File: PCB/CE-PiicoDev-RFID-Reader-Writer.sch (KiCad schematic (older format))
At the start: 59 parts, among them J1 , J2 , J3 Conn_01x06_Male, SW1 SW_DIP_x02, U1 MFRC522, Y1 27.12MHz 12pF

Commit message: Update
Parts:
- removed G4: Label_PCB_Art, PiicoDev RFID MFRC522:Label_Reset_Bar_Reverse Arrow, symbol CoreElectronics_Artwork:Label_PCB_Art
- removed G5: Label_PCB_Art, PiicoDev RFID MFRC522:Label_Reset_Bar, symbol CoreElectronics_Artwork:Label_PCB_Art
- U1: footprint Package_DFN_QFN:VQFN-32-1EP_5x5mm_P0.5mm_EP3.1x3.1mm -> Package_DFN_QFN:VQFN-32-1EP_5x5mm_P0.5mm_EP3.1x3.1mm_ThermalVias
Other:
- note removed: "~RST"
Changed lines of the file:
@@
 Sheet 1 1
 Title "PiicoDev RFID Reader/Writer MFRC522"
-Date "2021-12-14"
+Date "2021-12-21"
 Rev "03"
 Comp "Core Electronics"
@@
 	5450 1750 5850 1750
 Connection ~ 5850 1750
-$Comp
-L power:GND #PWR0112
-U 1 1 6156B677
-P 5100 2650
-F 0 "#PWR0112" H 5100 2400 50  0001 C CNN
-F 1 "GND" H 5105 2477 50  0000 C CNN
-F 2 "" H 5100 2650 50  0001 C CNN
-F 3 "" H 5100 2650 50  0001 C CNN
-	1    5100 2650
-	1    0    0    -1
-$EndComp
 Wire Wire Line
 	5100 2650 5100 2600
@@
 F 0 "U1" H 6050 1627 50  0000 C CNN
 F 1 "MFRC522" H 6050 1536 50  0000 C CNN
-F 2 "Package_DFN_QFN:VQFN-32-1EP_5x5mm_P0.5mm_EP3.1x3.1mm" H 5900 3350 50  0001 C CNN
+F 2 "Package_DFN_QFN:VQFN-32-1EP_5x5mm_P0.5mm_EP3.1x3.1mm_ThermalVias" H 5900 3350 50  0001 C CNN
 F 3 "https://www.nxp.com/docs/en/data-sheet/MFRC522.pdf" H 5900 3350 50  0001 C CNN
 	1    6050 3150
@@
 Text Label 10400 3150 0    50   ~ 0
 TURN6A
-$Comp
-L CoreElectronics_Artwork:Label_PCB_Art G4
-U 1 1 617897A9
-P 4150 6900
-F 0 "G4" H 4278 6946 50  0000 L CNN
-F 1 "Label_PCB_Art" H 4278 6855 50  0000 L CNN
-F 2 "PiicoDev RFID MFRC522:Label_Reset_Bar_Reverse Arrow" H 4150 6900 50  0001 C CNN
-F 3 "" H 4150 6900 50  0001 C CNN
-	1    4150 6900
-	1    0    0    -1
-$EndComp
-$Comp
-L CoreElectronics_Artwork:Label_PCB_Art G5
-U 1 1 6178A645
-P 4150 7150
-F 0 "G5" H 4278 7196 50  0000 L CNN
-F 1 "Label_PCB_Art" H 4278 7105 50  0000 L CNN
-F 2 "PiicoDev RFID MFRC522:Label_Reset_Bar" H 4150 7150 50  0001 C CNN
-F 3 "" H 4150 7150 50  0001 C CNN
-	1    4150 7150
-	1    0    0    -1
-$EndComp
-Text Notes 4050 6950 0    50   ~ 0
-~RST
-Text Notes 4050 7200 0    50   ~ 0
-~RST
 Text Notes 4050 5300 0    50   ~ 0
 f = 13.56 MHz\n\nCoil (as measured)\nL = 470 nH\nR = 0.3 ohm
@@
 U 1 1 61AFBFE8
 P 5100 2950
-F 0 "R11" V 4893 2950 50  0000 C CNN
-F 1 "120R" V 4984 2950 50  0000 C CNN
+F 0 "R11" V 5100 2950 50  0000 C CNN
+F 1 "120R" V 5200 2950 50  0000 C CNN
 F 2 "Resistor_SMD:R_0402_1005Metric" V 5030 2950 50  0001 C CNN
 F 3 "~" H 5100 2950 50  0001 C CNN
@@
 Wire Wire Line
 	2600 1800 2800 1800
+$Comp
+L power:GND #PWR0112
+U 1 1 6156B677
+P 5100 2650
+F 0 "#PWR0112" H 5100 2400 50  0001 C CNN
+F 1 "GND" H 5100 2500 50  0000 C CNN
+F 2 "" H 5100 2650 50  0001 C CNN
+F 3 "" H 5100 2650 50  0001 C CNN
+	1    5100 2650
+	1    0    0    -1
+$EndComp
 $EndSCHEMATC

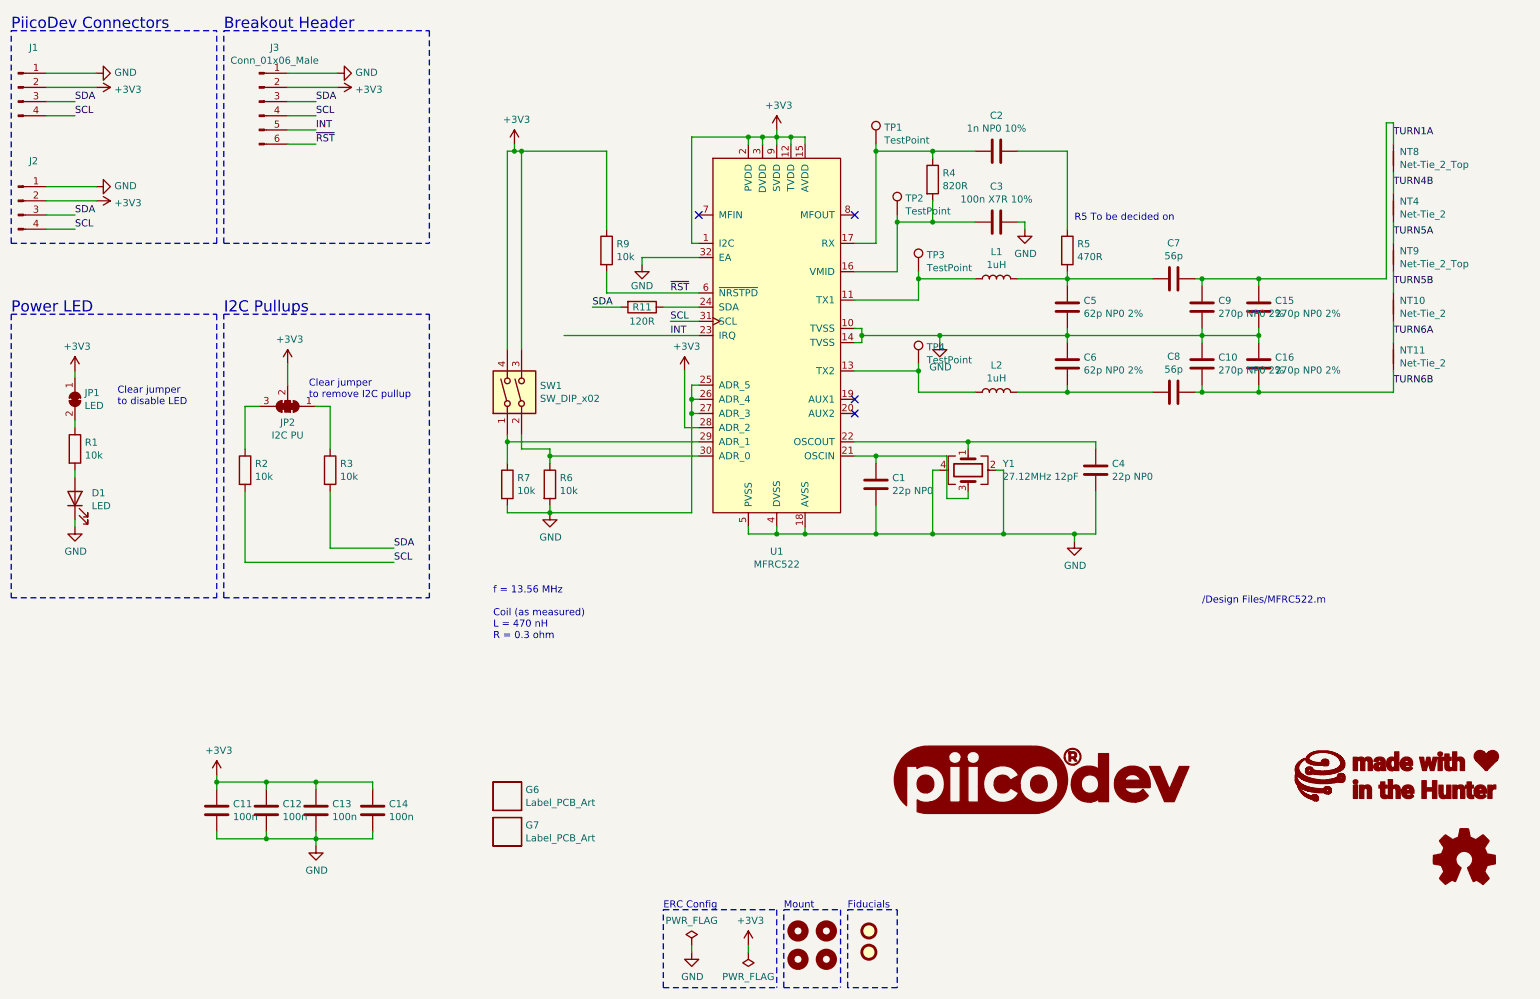
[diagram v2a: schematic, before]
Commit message: v10 Release
Remove testpoints
Change ASW order so SW1 is LSB
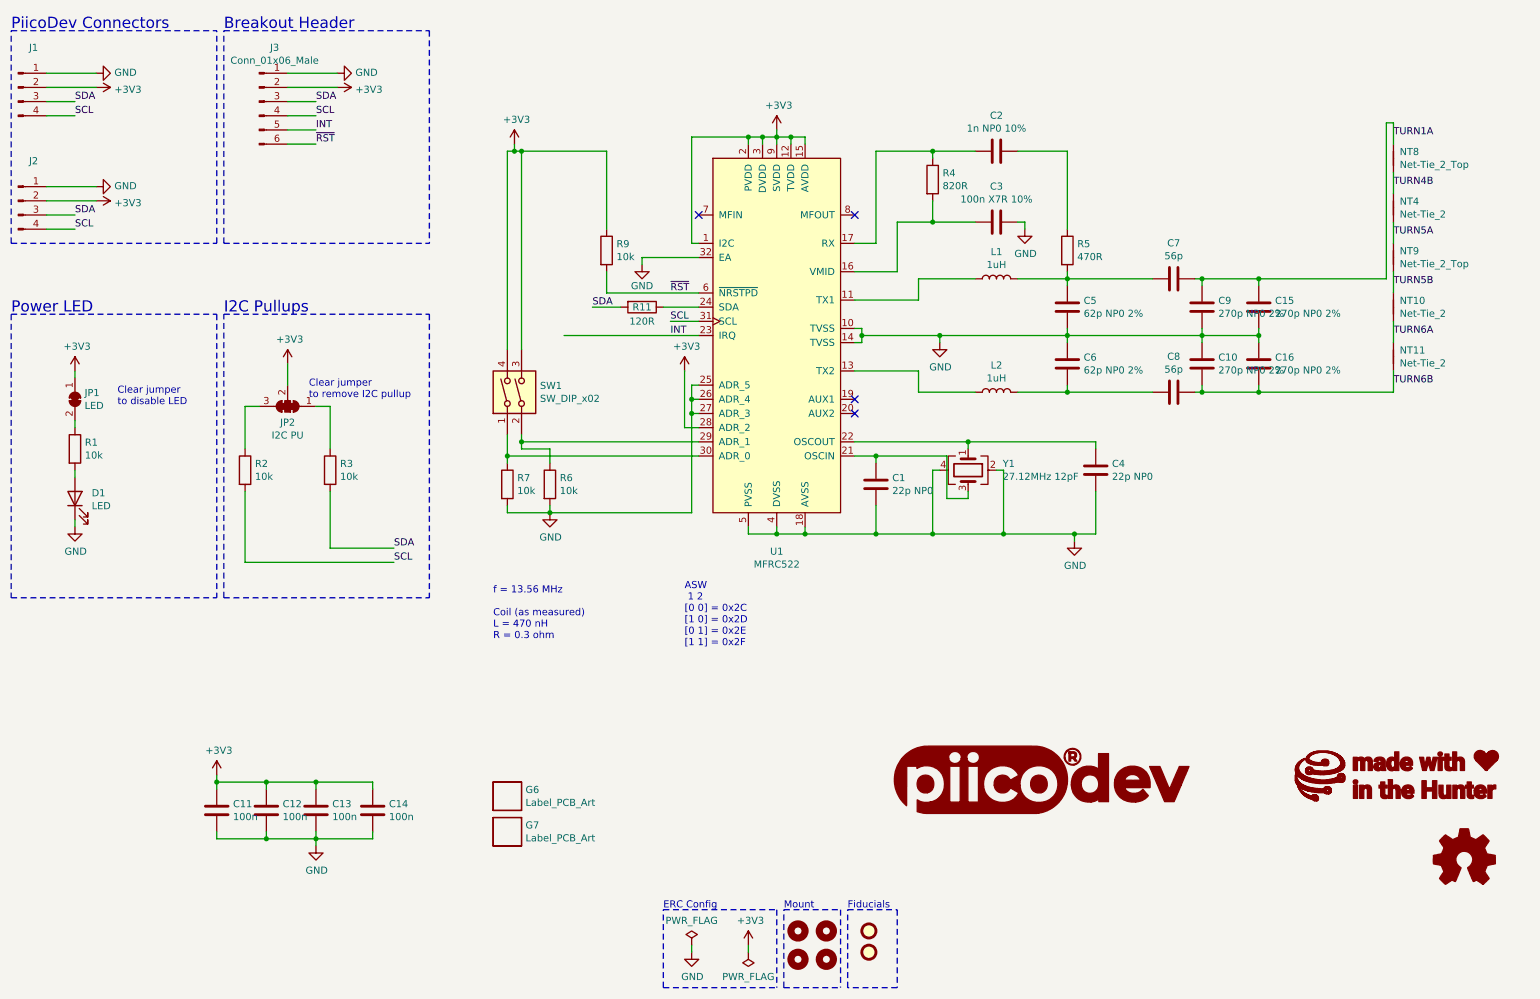
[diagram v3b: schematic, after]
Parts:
- removed TP1, TP2, TP3, TP4: TestPoint, CoreElectronics_Components:TestPoint_Pad_0.7x0.7mm, symbol Connector:TestPoint
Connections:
- net at R7.1, SW1.1: now also U1.30 (ADR_0); no longer U1.29 (ADR_1)
- net at R6.1, SW1.2: now also U1.29 (ADR_1); no longer U1.30 (ADR_0)
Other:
- note added: "ASW\n 1 2\n[0 0] = 0x2C\n[1 0] = 0x2D\n[0 1] = 0x2E\n[1 1] = 0x2F"
- note removed: "/Design Files/MFRC522.m"
- note removed: "R5 To be decided on"
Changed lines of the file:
@@
 encoding utf-8
 Sheet 1 1
-Title "PiicoDev RFID Reader/Writer MFRC522"
-Date "2021-12-23"
-Rev "04"
+Title "PiicoDev RFID Module"
+Date "2022-01-12"
+Rev "10"
 Comp "Core Electronics"
 Comment1 "Designed at Core Electronics by Peter Johnston"
@@
 Wire Wire Line
 	8100 3550 8700 3550
-Text Notes 8150 2350 0    50   ~ 0
-R5 To be decided on
 Wire Wire Line
 	6050 1750 6150 1750
@@
 Text Notes 4050 5300 0    50   ~ 0
 f = 13.56 MHz\n\nCoil (as measured)\nL = 470 nH\nR = 0.3 ohm
-Text Notes 9050 5050 0    50   ~ 0
-/Design Files/MFRC522.m
 Wire Wire Line
 	4850 2850 5500 2850
@@
 Wire Wire Line
 	4950 2950 4750 2950
-$Comp
-L Connector:TestPoint TP3
-U 1 1 618A1A4D
-P 7050 2700
-F 0 "TP3" H 7108 2818 50  0000 L CNN
-F 1 "TestPoint" H 7108 2727 50  0000 L CNN
-F 2 "CoreElectronics_Components:TestPoint_Pad_0.7x0.7mm" H 7250 2700 50  0001 C CNN
-F 3 "~" H 7250 2700 50  0001 C CNN
-	1    7050 2700
-	1    0    0    -1
-$EndComp
-$Comp
-L Connector:TestPoint TP4
-U 1 1 618A2E15
-P 7050 3350
-F 0 "TP4" H 7108 3468 50  0000 L CNN
-F 1 "TestPoint" H 7108 3377 50  0000 L CNN
-F 2 "CoreElectronics_Components:TestPoint_Pad_0.7x0.7mm" H 7250 3350 50  0001 C CNN
-F 3 "~" H 7250 3350 50  0001 C CNN
-	1    7050 3350
-	1    0    0    -1
-$EndComp
-Wire Wire Line
-	7050 2700 7050 2750
-Connection ~ 7050 2750
-Wire Wire Line
-	7050 3350 7050 3400
-Connection ~ 7050 3400
-$Comp
-L Connector:TestPoint TP1
-U 1 1 618B17E8
-P 6750 1800
-F 0 "TP1" H 6808 1918 50  0000 L CNN
-F 1 "TestPoint" H 6808 1827 50  0000 L CNN
-F 2 "CoreElectronics_Components:TestPoint_Pad_0.7x0.7mm" H 6950 1800 50  0001 C CNN
-F 3 "~" H 6950 1800 50  0001 C CNN
-	1    6750 1800
-	1    0    0    -1
-$EndComp
-Wire Wire Line
-	6750 1800 6750 1850
-Connection ~ 6750 1850
-$Comp
-L Connector:TestPoint TP2
-U 1 1 618B9830
-P 6900 2300
-F 0 "TP2" H 6958 2418 50  0000 L CNN
-F 1 "TestPoint" H 6958 2327 50  0000 L CNN
-F 2 "CoreElectronics_Components:TestPoint_Pad_0.7x0.7mm" H 7100 2300 50  0001 C CNN
-F 3 "~" H 7100 2300 50  0001 C CNN
-	1    6900 2300
-	1    0    0    -1
-$EndComp
-Wire Wire Line
-	6900 2300 6900 2350
-Connection ~ 6900 2350
 Wire Wire Line
 	5500 3500 5450 3500
@@
 $EndComp
 Wire Wire Line
-	5500 4000 4450 4000
-Wire Wire Line
-	4450 4000 4450 4050
-Wire Wire Line
 	4450 4350 4450 4400
-Connection ~ 4450 4000
 $Comp
 L CoreElectronics_Artwork:Label_PCB_Art G7
@@
 	4250 1850 4850 1850
 Wire Wire Line
-	4150 3850 4150 3900
-Wire Wire Line
-	4150 3900 4150 4050
-Connection ~ 4150 3900
-Wire Wire Line
-	4250 3850 4250 3950
+	4250 3850 4250 3900
 Wire Wire Line
 	4250 3950 4450 3950
-Wire Wire Line
-	4450 3950 4450 4000
-Wire Wire Line
-	4150 3900 5500 3900
 Wire Wire Line
 	5450 3700 5450 4400
@@
 	1    0    0    -1
 $EndComp
+Text Notes 5400 5350 0    50   ~ 0
+ ASW\n 1 2\n[0 0] = 0x2C\n[1 0] = 0x2D\n[0 1] = 0x2E\n[1 1] = 0x2F
+Wire Wire Line
+	4450 3950 4450 4050
+Wire Wire Line
+	5500 4000 4150 4000
+Connection ~ 4150 4000
+Wire Wire Line
+	4150 4000 4150 4050
+Wire Wire Line
+	4150 3850 4150 4000
+Wire Wire Line
+	5500 3900 4250 3900
+Connection ~ 4250 3900
+Wire Wire Line
+	4250 3900 4250 3950
 $EndSCHEMATC

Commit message: Change R5 to 1k
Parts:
- R5: value 470R -> 1k
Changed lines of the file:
@@
 P 8100 2550
 F 0 "R5" H 8170 2596 50  0000 L CNN
-F 1 "470R" H 8170 2505 50  0000 L CNN
+F 1 "1k" H 8170 2505 50  0000 L CNN
 F 2 "Resistor_SMD:R_0603_1608Metric" V 8030 2550 50  0001 C CNN
 F 3 "~" H 8100 2550 50  0001 C CNN

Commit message: Add schematic.pdf and schematic comments
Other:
- note added: "ASW I2C ADDR\n 1 2\n[0 0] = 0x2C\n[1 0] = 0x2D\n[0 1] = 0x2E\n[1 1] = 0x2F"
- note added: "Net ties allow coil dimensions\nto be prescribed in PCB layout"
- note removed: "ASW\n 1 2\n[0 0] = 0x2C\n[1 0] = 0x2D\n[0 1] = 0x2E\n[1 1] = 0x2F"
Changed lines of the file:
@@
 P 5450 7450
 AR Path="/609C5735/609C9ECA" Ref="#FLG?"  Part="1"
-AR Path="/609C9ECA" Ref="#FLG0101"  Part="1"
-F 0 "#FLG0101" H 5450 7525 50  0001 C CNN
+AR Path="/609C9ECA" Ref="#FLG?"  Part="1"
+F 0 "#FLG?" H 5450 7525 50  0001 C CNN
 F 1 "PWR_FLAG" H 5450 7623 50  0000 C CNN
 F 2 "" H 5450 7450 50  0001 C CNN
@@
 P 5850 7500
 AR Path="/609C5735/609C9ED0" Ref="#FLG?"  Part="1"
-AR Path="/609C9ED0" Ref="#FLG0102"  Part="1"
-F 0 "#FLG0102" H 5850 7575 50  0001 C CNN
+AR Path="/609C9ED0" Ref="#FLG?"  Part="1"
+F 0 "#FLG?" H 5850 7575 50  0001 C CNN
 F 1 "PWR_FLAG" H 5850 7673 50  0000 C CNN
 F 2 "" H 5850 7500 50  0001 C CNN
@@
 P 5450 7500
 AR Path="/609C5735/609C9ED6" Ref="#PWR?"  Part="1"
-AR Path="/609C9ED6" Ref="#PWR0101"  Part="1"
-F 0 "#PWR0101" H 5450 7250 50  0001 C CNN
+AR Path="/609C9ED6" Ref="#PWR?"  Part="1"
+F 0 "#PWR?" H 5450 7250 50  0001 C CNN
 F 1 "GND" H 5455 7327 50  0000 C CNN
 F 2 "" H 5450 7500 50  0001 C CNN
@@
 P 5850 7450
 AR Path="/609C5735/609C9EDC" Ref="#PWR?"  Part="1"
-AR Path="/609C9EDC" Ref="#PWR0102"  Part="1"
-F 0 "#PWR0102" H 5850 7300 50  0001 C CNN
+AR Path="/609C9EDC" Ref="#PWR?"  Part="1"
+F 0 "#PWR?" H 5850 7300 50  0001 C CNN
 F 1 "+3V3" H 5865 7623 50  0000 C CNN
 F 2 "" H 5850 7450 50  0001 C CNN
@@
 P 1250 1400
 AR Path="/609C5735/609F9AF4" Ref="#PWR?"  Part="1"
-AR Path="/609F9AF4" Ref="#PWR0103"  Part="1"
-F 0 "#PWR0103" H 1250 1250 50  0001 C CNN
+AR Path="/609F9AF4" Ref="#PWR?"  Part="1"
+F 0 "#PWR?" H 1250 1250 50  0001 C CNN
 F 1 "+3V3" V 1265 1528 50  0000 L CNN
 F 2 "" H 1250 1400 50  0001 C CNN
@@
 P 1250 1300
 AR Path="/609C5735/609F9AFA" Ref="#PWR?"  Part="1"
-AR Path="/609F9AFA" Ref="#PWR0104"  Part="1"
-F 0 "#PWR0104" H 1250 1050 50  0001 C CNN
+AR Path="/609F9AFA" Ref="#PWR?"  Part="1"
+F 0 "#PWR?" H 1250 1050 50  0001 C CNN
 F 1 "GND" V 1255 1172 50  0000 R CNN
 F 2 "" H 1250 1300 50  0001 C CNN
@@
 P 1250 2200
 AR Path="/609C5735/609F9B0C" Ref="#PWR?"  Part="1"
-AR Path="/609F9B0C" Ref="#PWR0105"  Part="1"
-F 0 "#PWR0105" H 1250 2050 50  0001 C CNN
+AR Path="/609F9B0C" Ref="#PWR?"  Part="1"
+F 0 "#PWR?" H 1250 2050 50  0001 C CNN
 F 1 "+3V3" V 1265 2328 50  0000 L CNN
 F 2 "" H 1250 2200 50  0001 C CNN
@@
 P 1250 2100
 AR Path="/609C5735/609F9B12" Ref="#PWR?"  Part="1"
-AR Path="/609F9B12" Ref="#PWR0106"  Part="1"
-F 0 "#PWR0106" H 1250 1850 50  0001 C CNN
+AR Path="/609F9B12" Ref="#PWR?"  Part="1"
+F 0 "#PWR?" H 1250 1850 50  0001 C CNN
 F 1 "GND" V 1255 1972 50  0000 R CNN
 F 2 "" H 1250 2100 50  0001 C CNN
@@
 P 2950 1400
 AR Path="/609C5735/609F9B1E" Ref="#PWR?"  Part="1"
-AR Path="/609F9B1E" Ref="#PWR0107"  Part="1"
-F 0 "#PWR0107" H 2950 1250 50  0001 C CNN
+AR Path="/609F9B1E" Ref="#PWR?"  Part="1"
+F 0 "#PWR?" H 2950 1250 50  0001 C CNN
 F 1 "+3V3" V 2965 1528 50  0000 L CNN
 F 2 "" H 2950 1400 50  0001 C CNN
@@
 P 2950 1300
 AR Path="/609C5735/609F9B24" Ref="#PWR?"  Part="1"
-AR Path="/609F9B24" Ref="#PWR0108"  Part="1"
-F 0 "#PWR0108" H 2950 1050 50  0001 C CNN
+AR Path="/609F9B24" Ref="#PWR?"  Part="1"
+F 0 "#PWR?" H 2950 1050 50  0001 C CNN
 F 1 "GND" V 2955 1172 50  0000 R CNN
 F 2 "" H 2950 1300 50  0001 C CNN
@@
 P 2600 3350
 AR Path="/609C5735/60A0817C" Ref="#PWR?"  Part="1"
-AR Path="/60A0817C" Ref="#PWR0109"  Part="1"
-F 0 "#PWR0109" H 2600 3200 50  0001 C CNN
+AR Path="/60A0817C" Ref="#PWR?"  Part="1"
+F 0 "#PWR?" H 2600 3200 50  0001 C CNN
 F 1 "+3V3" H 2615 3523 50  0000 C CNN
 F 2 "" H 2600 3350 50  0001 C CNN
@@
 $EndComp
 $Comp
-L power:GND #PWR0110
+L power:GND #PWR?
 U 1 1 60A1F608
 P 1100 4500
-F 0 "#PWR0110" H 1100 4250 50  0001 C CNN
+F 0 "#PWR?" H 1100 4250 50  0001 C CNN
 F 1 "GND" H 1105 4327 50  0000 C CNN
 F 2 "" H 1100 4500 50  0001 C CNN
@@
 	1100 4500 1100 4450
 $Comp
-L power:+3V3 #PWR0111
+L power:+3V3 #PWR?
 U 1 1 60A1F60F
 P 1100 3400
-F 0 "#PWR0111" H 1100 3250 50  0001 C CNN
+F 0 "#PWR?" H 1100 3250 50  0001 C CNN
 F 1 "+3V3" H 1115 3573 50  0000 C CNN
 F 2 "" H 1100 3400 50  0001 C CNN
@@
 Connection ~ 6050 4550
 $Comp
-L power:GND #PWR04
+L power:GND #PWR?
 U 1 1 6138CEF8
 P 8150 4600
-F 0 "#PWR04" H 8150 4350 50  0001 C CNN
+F 0 "#PWR?" H 8150 4350 50  0001 C CNN
 F 1 "GND" H 8155 4427 50  0000 C CNN
 F 2 "" H 8150 4600 50  0001 C CNN
@@
 Connection ~ 6050 1750
 $Comp
-L power:+3V3 #PWR01
+L power:+3V3 #PWR?
 U 1 1 6139367C
 P 6050 1700
-F 0 "#PWR01" H 6050 1550 50  0001 C CNN
+F 0 "#PWR?" H 6050 1550 50  0001 C CNN
 F 1 "+3V3" H 6065 1873 50  0000 C CNN
 F 2 "" H 6050 1700 50  0001 C CNN
@@
 	7150 2200 7150 2350
 $Comp
-L power:GND #PWR03
+L power:GND #PWR?
 U 1 1 6143980E
 P 7800 2400
-F 0 "#PWR03" H 7800 2150 50  0001 C CNN
+F 0 "#PWR?" H 7800 2150 50  0001 C CNN
 F 1 "GND" H 7805 2227 50  0000 C CNN
 F 2 "" H 7800 2400 50  0001 C CNN
@@
 $EndComp
 $Comp
-L power:GND #PWR02
+L power:GND #PWR?
 U 1 1 614797C1
 P 7200 3200
-F 0 "#PWR02" H 7200 2950 50  0001 C CNN
+F 0 "#PWR?" H 7200 2950 50  0001 C CNN
 F 1 "GND" H 7205 3027 50  0000 C CNN
 F 2 "" H 7200 3200 50  0001 C CNN
@@
 Connection ~ 8150 4550
 $Comp
-L power:+3V3 #PWR0113
+L power:+3V3 #PWR?
 U 1 1 613921B9
 P 4200 1800
-F 0 "#PWR0113" H 4200 1650 50  0001 C CNN
+F 0 "#PWR?" H 4200 1650 50  0001 C CNN
 F 1 "+3V3" H 4215 1973 50  0000 C CNN
 F 2 "" H 4200 1800 50  0001 C CNN
@@
 	4200 1800 4200 1850
 $Comp
-L power:GND #PWR0114
+L power:GND #PWR?
 U 1 1 613BD9A7
 P 2800 6750
-F 0 "#PWR0114" H 2800 6500 50  0001 C CNN
+F 0 "#PWR?" H 2800 6500 50  0001 C CNN
 F 1 "GND" H 2805 6577 50  0000 C CNN
 F 2 "" H 2800 6750 50  0001 C CNN
@@
 	6150 1750 6250 1750
 $Comp
-L power:+3V3 #PWR0115
+L power:+3V3 #PWR?
 U 1 1 613CB708
 P 2100 6250
-F 0 "#PWR0115" H 2100 6100 50  0001 C CNN
+F 0 "#PWR?" H 2100 6100 50  0001 C CNN
 F 1 "+3V3" H 2115 6423 50  0000 C CNN
 F 2 "" H 2100 6250 50  0001 C CNN
@@
 	5500 3800 5400 3800
 $Comp
-L power:+3V3 #PWR0117
+L power:+3V3 #PWR?
 U 1 1 61A856C1
 P 5400 3400
-F 0 "#PWR0117" H 5400 3250 50  0001 C CNN
+F 0 "#PWR?" H 5400 3250 50  0001 C CNN
 F 1 "+3V3" H 5415 3573 50  0000 C CNN
 F 2 "" H 5400 3400 50  0001 C CNN
@@
 $EndComp
 $Comp
-L power:GND #PWR0118
+L power:GND #PWR?
 U 1 1 61A92E3B
 P 4450 4400
-F 0 "#PWR0118" H 4450 4150 50  0001 C CNN
+F 0 "#PWR?" H 4450 4150 50  0001 C CNN
 F 1 "GND" H 4455 4227 50  0000 C CNN
 F 2 "" H 4450 4400 50  0001 C CNN
@@
 $EndComp
 Wire Wire Line
-	4550 3150 5500 3150
-Wire Wire Line
 	5400 3400 5400 3800
 $Comp
@@
 	2600 1800 2800 1800
 $Comp
-L power:GND #PWR0112
+L power:GND #PWR?
 U 1 1 6156B677
 P 5100 2650
-F 0 "#PWR0112" H 5100 2400 50  0001 C CNN
+F 0 "#PWR?" H 5100 2400 50  0001 C CNN
 F 1 "GND" H 5100 2500 50  0000 C CNN
 F 2 "" H 5100 2650 50  0001 C CNN
@@
 $EndComp
 Text Notes 5400 5350 0    50   ~ 0
- ASW\n 1 2\n[0 0] = 0x2C\n[1 0] = 0x2D\n[0 1] = 0x2E\n[1 1] = 0x2F
+ ASW   I2C ADDR\n 1 2\n[0 0] = 0x2C\n[1 0] = 0x2D\n[0 1] = 0x2E\n[1 1] = 0x2F
 Wire Wire Line
 	4450 3950 4450 4050
@@
 Wire Wire Line
 	4250 3900 4250 3950
+Text Notes 9900 1550 0    50   ~ 0
+Net ties allow coil dimensions\nto be prescribed in PCB layout
+Wire Wire Line
+	5300 3150 5500 3150
 $EndSCHEMATC
